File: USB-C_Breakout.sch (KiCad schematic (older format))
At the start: 4 parts

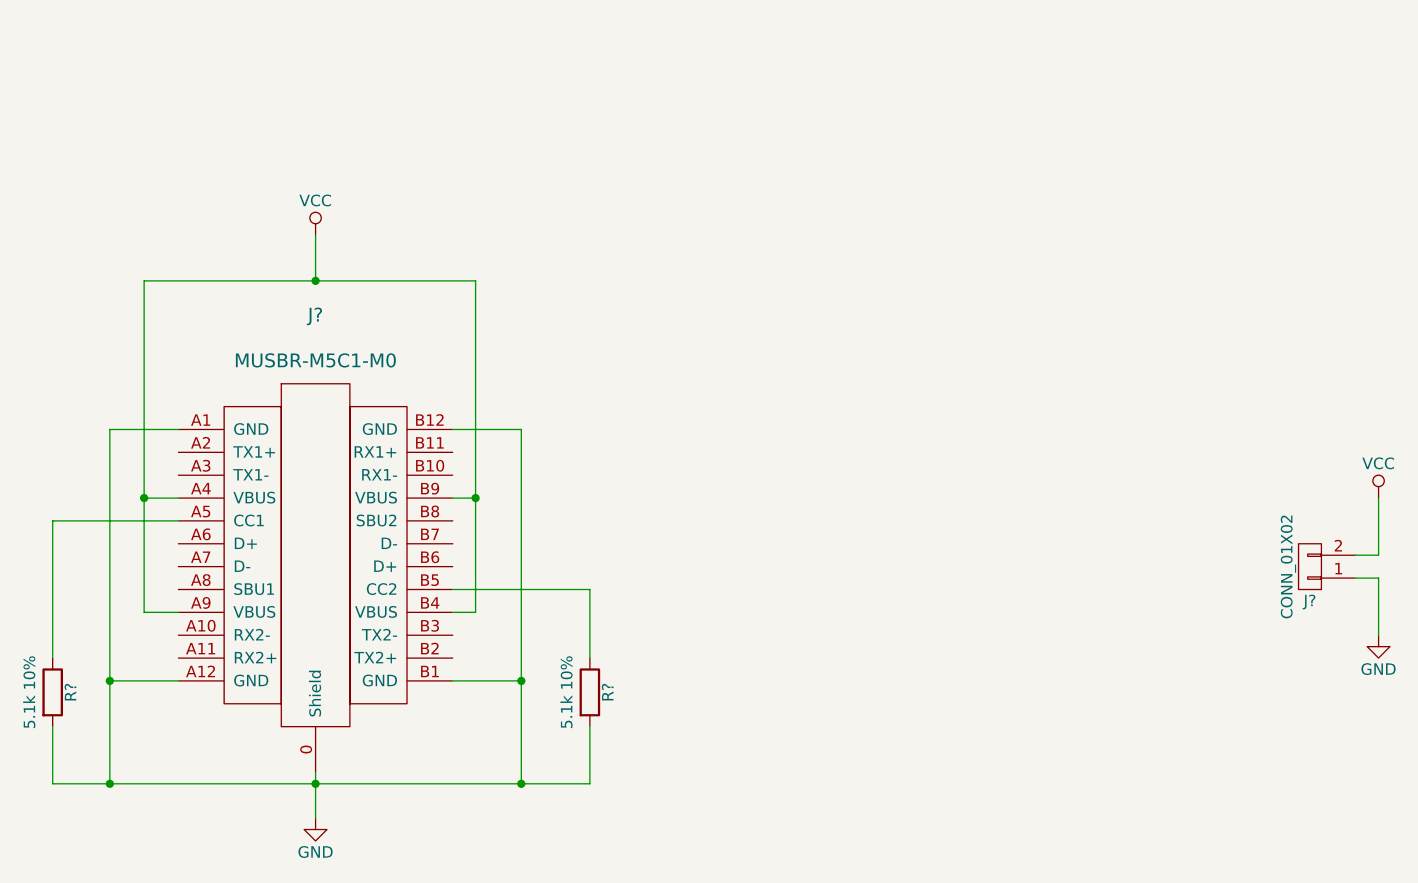
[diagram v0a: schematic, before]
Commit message: Updated Footprints
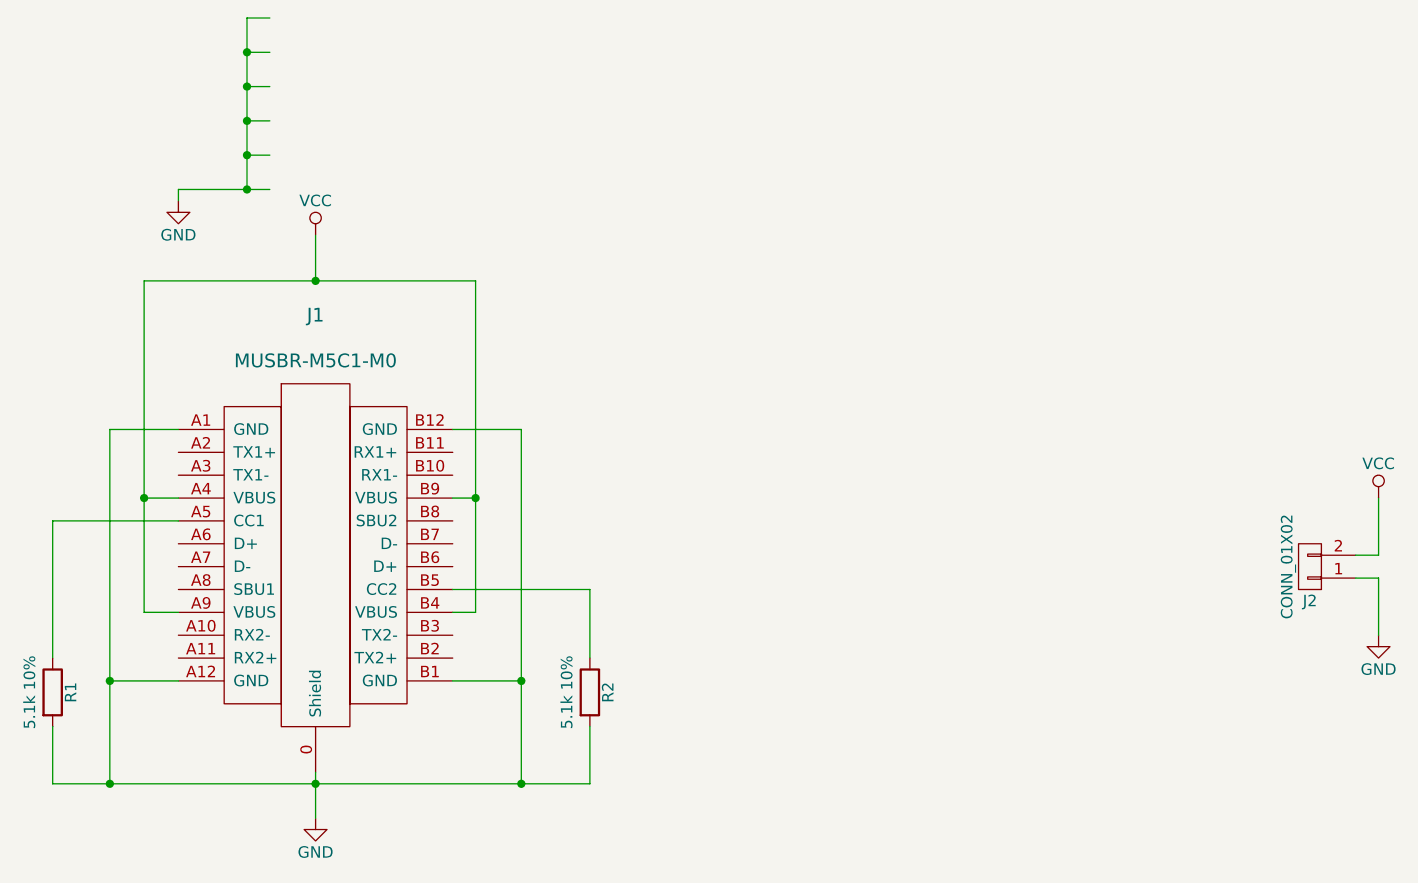
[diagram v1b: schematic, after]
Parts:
- removed R?: 5.1k 10%, symbol R
- added R1: 5.1k 10%, Resistors_SMD:R_0805, symbol R
- J1: renamed from J?; footprint (none) -> MUSBR-M5C1-X0:MUSBR-M5C1-X0
- J2: renamed from J?; footprint (none) -> 640455-2:640455-2
- R2: renamed from R?; footprint (none) -> Resistors_SMD:R_0805
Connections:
- net GND: now also J1.G1 (GND), J1.G2 (GND), J1.G3 (GND), J1.G4 (GND), J1.G5 (GND), J1.G6 (GND), R1.2
- net at J1.A5 (CC1): now also R1.1
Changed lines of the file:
@@
 LIBS:power
 LIBS:device
-LIBS:transistors
-LIBS:conn
-LIBS:linear
-LIBS:regul
 LIBS:74xx
-LIBS:cmos4000
-LIBS:adc-dac
-LIBS:memory
-LIBS:xilinx
-LIBS:microcontrollers
-LIBS:dsp
-LIBS:microchip
-LIBS:analog_switches
-LIBS:motorola
-LIBS:texas
-LIBS:intel
 LIBS:audio
 LIBS:interface
-LIBS:digital-audio
-LIBS:philips
-LIBS:display
-LIBS:cypress
-LIBS:siliconi
-LIBS:opto
-LIBS:atmel
-LIBS:contrib
-LIBS:valves
 LIBS:usb-type-c
+LIBS:USB-C_Breakout-cache
 EELAYER 25 0
 EELAYER END
@@
 $EndDescr
 $Comp
-L USB_TYPE_C J?
+L USB_TYPE_C J1
 U 1 1 5AC3DA60
 P 3550 3350
-F 0 "J?" H 3550 4400 60  0000 C CNN
+F 0 "J1" H 3550 4400 60  0000 C CNN
 F 1 "MUSBR-M5C1-M0" H 3550 4200 60  0000 C CNN
-F 2 "" H 3550 3350 60  0000 C CNN
+F 2 "MUSBR-M5C1-X0:MUSBR-M5C1-X0" H 3550 3350 60  0001 C CNN
 F 3 "" H 3550 3350 60  0000 C CNN
 	1    3550 3350
@@
 $EndComp
 $Comp
-L CONN_01X02 J?
+L CONN_01X02 J2
 U 1 1 5AC3DB4D
 P 7900 3400
-F 0 "J?" H 7900 3550 50  0000 C CNN
+F 0 "J2" H 7900 3550 50  0000 C CNN
 F 1 "CONN_01X02" V 8000 3400 50  0000 C CNN
-F 2 "" H 7900 3400 50  0001 C CNN
+F 2 "640455-2:640455-2" H 7900 3400 50  0001 C CNN
 F 3 "" H 7900 3400 50  0001 C CNN
 	1    7900 3400
@@
 $EndComp
 $Comp
-L R R?
+L R R2
 U 1 1 5AC3DBB4
 P 4750 3950
-F 0 "R?" V 4830 3950 50  0000 C CNN
+F 0 "R2" V 4830 3950 50  0000 C CNN
 F 1 "5.1k 10%" V 4650 3950 50  0000 C CNN
-F 2 "" V 4680 3950 50  0001 C CNN
+F 2 "Resistors_SMD:R_0805" V 4680 3950 50  0001 C CNN
 F 3 "" H 4750 3950 50  0001 C CNN
 	1    4750 3950
@@
 $EndComp
 $Comp
-L VCC #PWR?
+L VCC #PWR2
 U 1 1 5AC3DC66
 P 3550 1950
-F 0 "#PWR?" H 3550 1800 50  0001 C CNN
+F 0 "#PWR2" H 3550 1800 50  0001 C CNN
 F 1 "VCC" H 3550 2100 50  0000 C CNN
 F 2 "" H 3550 1950 50  0001 C CNN
@@
 $EndComp
 $Comp
-L GND #PWR?
+L GND #PWR3
 U 1 1 5AC3DCE0
 P 3550 4500
-F 0 "#PWR?" H 3550 4250 50  0001 C CNN
+F 0 "#PWR3" H 3550 4250 50  0001 C CNN
 F 1 "GND" H 3550 4350 50  0000 C CNN
 F 2 "" H 3550 4500 50  0001 C CNN
@@
 	1    0    0    -1
 $EndComp
-$Comp
-L R R?
-U 1 1 5AC3DFFC
-P 2400 3950
-F 0 "R?" V 2480 3950 50  0000 C CNN
-F 1 "5.1k 10%" V 2300 3950 50  0000 C CNN
-F 2 "" V 2330 3950 50  0001 C CNN
-F 3 "" H 2400 3950 50  0001 C CNN
-	1    2400 3950
-	1    0    0    -1
-$EndComp
 Wire Wire Line
 	3550 4300 3550 4500
@@
 Connection ~ 2650 4350
 $Comp
-L VCC #PWR?
+L VCC #PWR4
 U 1 1 5AC3E2BC
 P 8200 3100
-F 0 "#PWR?" H 8200 2950 50  0001 C CNN
+F 0 "#PWR4" H 8200 2950 50  0001 C CNN
 F 1 "VCC" H 8200 3250 50  0000 C CNN
 F 2 "" H 8200 3100 50  0001 C CNN
@@
 $EndComp
 $Comp
-L GND #PWR?
+L GND #PWR5
 U 1 1 5AC3E2D3
 P 8200 3700
-F 0 "#PWR?" H 8200 3450 50  0001 C CNN
+F 0 "#PWR5" H 8200 3450 50  0001 C CNN
 F 1 "GND" H 8200 3550 50  0000 C CNN
 F 2 "" H 8200 3700 50  0001 C CNN
@@
 Wire Wire Line
 	8200 3450 8200 3700
+$Comp
+L R R1
+U 1 1 5AC3F2EA
+P 2400 3950
+F 0 "R1" V 2480 3950 50  0000 C CNN
+F 1 "5.1k 10%" V 2300 3950 50  0000 C CNN
+F 2 "Resistors_SMD:R_0805" V 2330 3950 50  0001 C CNN
+F 3 "" H 2400 3950 50  0001 C CNN
+	1    2400 3950
+	1    0    0    -1
+$EndComp
+$Comp
+L GND #PWR1
+U 1 1 5AC400B5
+P 2950 1800
+F 0 "#PWR1" H 2950 1550 50  0001 C CNN
+F 1 "GND" H 2950 1650 50  0000 C CNN
+F 2 "" H 2950 1800 50  0001 C CNN
+F 3 "" H 2950 1800 50  0001 C CNN
+	1    2950 1800
+	1    0    0    -1
+$EndComp
+Wire Wire Line
+	3350 1750 2950 1750
+Wire Wire Line
+	2950 1750 2950 1800
+Wire Wire Line
+	3350 1600 3250 1600
+Wire Wire Line
+	3250 1000 3250 1750
+Connection ~ 3250 1750
+Wire Wire Line
+	3350 1450 3250 1450
+Connection ~ 3250 1600
+Wire Wire Line
+	3350 1300 3250 1300
+Connection ~ 3250 1450
+Wire Wire Line
+	3350 1150 3250 1150
+Connection ~ 3250 1300
+Wire Wire Line
+	3350 1000 3250 1000
+Connection ~ 3250 1150
 $EndSCHEMATC

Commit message: Initial Release of Rev A
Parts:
- J2: value CONN_01X02 -> 640455-2
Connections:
- net GND: no longer J1.G1 (GND), J1.G2 (GND), J1.G3 (GND), J1.G4 (GND), J1.G5 (GND), J1.G6 (GND)
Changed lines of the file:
@@
 LIBS:power
 LIBS:device
+LIBS:transistors
+LIBS:conn
+LIBS:linear
+LIBS:regul
 LIBS:74xx
+LIBS:cmos4000
+LIBS:adc-dac
+LIBS:memory
+LIBS:xilinx
+LIBS:microcontrollers
+LIBS:dsp
+LIBS:microchip
+LIBS:analog_switches
+LIBS:motorola
+LIBS:texas
+LIBS:intel
 LIBS:audio
 LIBS:interface
+LIBS:digital-audio
+LIBS:philips
+LIBS:display
+LIBS:cypress
+LIBS:siliconi
+LIBS:opto
+LIBS:atmel
+LIBS:contrib
+LIBS:valves
 LIBS:usb-type-c
 LIBS:USB-C_Breakout-cache
@@
 $EndDescr
 $Comp
+L CONN_01X02 J2
+U 1 1 5AC3DB4D
+P 7900 3400
+F 0 "J2" H 7900 3550 50  0000 C CNN
+F 1 "640455-2" V 8000 3400 50  0000 C CNN
+F 2 "640455-2:640455-2" H 7900 3400 50  0001 C CNN
+F 3 "" H 7900 3400 50  0001 C CNN
+	1    7900 3400
+	-1   0    0    1
+$EndComp
+$Comp
+L R R2
+U 1 1 5AC3DBB4
+P 4750 3950
+F 0 "R2" V 4830 3950 50  0000 C CNN
+F 1 "5.1k 10%" V 4650 3950 50  0000 C CNN
+F 2 "Resistors_SMD:R_0805" V 4680 3950 50  0001 C CNN
+F 3 "" H 4750 3950 50  0001 C CNN
+	1    4750 3950
+	1    0    0    -1
+$EndComp
+$Comp
+L VCC #PWR01
+U 1 1 5AC3DC66
+P 3550 1950
+F 0 "#PWR01" H 3550 1800 50  0001 C CNN
+F 1 "VCC" H 3550 2100 50  0000 C CNN
+F 2 "" H 3550 1950 50  0001 C CNN
+F 3 "" H 3550 1950 50  0001 C CNN
+	1    3550 1950
+	1    0    0    -1
+$EndComp
+$Comp
+L GND #PWR02
+U 1 1 5AC3DCE0
+P 3550 4500
+F 0 "#PWR02" H 3550 4250 50  0001 C CNN
+F 1 "GND" H 3550 4350 50  0000 C CNN
+F 2 "" H 3550 4500 50  0001 C CNN
+F 3 "" H 3550 4500 50  0001 C CNN
+	1    3550 4500
+	1    0    0    -1
+$EndComp
+Wire Wire Line
+	3550 4300 3550 4500
+Wire Wire Line
+	4150 2800 4450 2800
+Wire Wire Line
+	4450 2800 4450 4350
+Wire Wire Line
+	2400 4350 4750 4350
+Connection ~ 3550 4350
+Wire Wire Line
+	2650 2800 2650 4350
+Wire Wire Line
+	2650 2800 2950 2800
+Wire Wire Line
+	4150 3900 4450 3900
+Connection ~ 4450 3900
+Wire Wire Line
+	2950 3900 2650 3900
+Connection ~ 2650 3900
+Wire Wire Line
+	4150 3100 4250 3100
+Wire Wire Line
+	4250 2150 4250 3600
+Wire Wire Line
+	2800 2150 4250 2150
+Wire Wire Line
+	3550 2150 3550 1950
+Wire Wire Line
+	2950 3100 2800 3100
+Wire Wire Line
+	2800 2150 2800 3600
+Connection ~ 3550 2150
+Wire Wire Line
+	4250 3600 4150 3600
+Connection ~ 4250 3100
+Wire Wire Line
+	2800 3600 2950 3600
+Connection ~ 2800 3100
+Wire Wire Line
+	4150 3500 4750 3500
+Wire Wire Line
+	4750 3500 4750 3800
+Wire Wire Line
+	4750 4350 4750 4100
+Connection ~ 4450 4350
+Wire Wire Line
+	2950 3200 2400 3200
+Wire Wire Line
+	2400 3200 2400 3800
+Wire Wire Line
+	2400 4100 2400 4350
+Connection ~ 2650 4350
+$Comp
+L VCC #PWR03
+U 1 1 5AC3E2BC
+P 8200 3100
+F 0 "#PWR03" H 8200 2950 50  0001 C CNN
+F 1 "VCC" H 8200 3250 50  0000 C CNN
+F 2 "" H 8200 3100 50  0001 C CNN
+F 3 "" H 8200 3100 50  0001 C CNN
+	1    8200 3100
+	1    0    0    -1
+$EndComp
+$Comp
+L GND #PWR04
+U 1 1 5AC3E2D3
+P 8200 3700
+F 0 "#PWR04" H 8200 3450 50  0001 C CNN
+F 1 "GND" H 8200 3550 50  0000 C CNN
+F 2 "" H 8200 3700 50  0001 C CNN
+F 3 "" H 8200 3700 50  0001 C CNN
+	1    8200 3700
+	1    0    0    -1
+$EndComp
+Wire Wire Line
+	8100 3350 8200 3350
+Wire Wire Line
+	8200 3350 8200 3100
+Wire Wire Line
+	8100 3450 8200 3450
+Wire Wire Line
+	8200 3450 8200 3700
+$Comp
+L R R1
+U 1 1 5AC3F2EA
+P 2400 3950
+F 0 "R1" V 2480 3950 50  0000 C CNN
+F 1 "5.1k 10%" V 2300 3950 50  0000 C CNN
+F 2 "Resistors_SMD:R_0805" V 2330 3950 50  0001 C CNN
+F 3 "" H 2400 3950 50  0001 C CNN
+	1    2400 3950
+	1    0    0    -1
+$EndComp
+$Comp
 L USB_TYPE_C J1
 U 1 1 5AC3DA60
@@
 $EndComp
 $Comp
-L CONN_01X02 J2
-U 1 1 5AC3DB4D
-P 7900 3400
-F 0 "J2" H 7900 3550 50  0000 C CNN
-F 1 "CONN_01X02" V 8000 3400 50  0000 C CNN
-F 2 "640455-2:640455-2" H 7900 3400 50  0001 C CNN
-F 3 "" H 7900 3400 50  0001 C CNN
-	1    7900 3400
-	-1   0    0    1
-$EndComp
-$Comp
-L R R2
-U 1 1 5AC3DBB4
-P 4750 3950
-F 0 "R2" V 4830 3950 50  0000 C CNN
-F 1 "5.1k 10%" V 4650 3950 50  0000 C CNN
-F 2 "Resistors_SMD:R_0805" V 4680 3950 50  0001 C CNN
-F 3 "" H 4750 3950 50  0001 C CNN
-	1    4750 3950
-	1    0    0    -1
-$EndComp
-$Comp
-L VCC #PWR2
-U 1 1 5AC3DC66
-P 3550 1950
-F 0 "#PWR2" H 3550 1800 50  0001 C CNN
-F 1 "VCC" H 3550 2100 50  0000 C CNN
-F 2 "" H 3550 1950 50  0001 C CNN
-F 3 "" H 3550 1950 50  0001 C CNN
-	1    3550 1950
-	1    0    0    -1
-$EndComp
-$Comp
-L GND #PWR3
-U 1 1 5AC3DCE0
-P 3550 4500
-F 0 "#PWR3" H 3550 4250 50  0001 C CNN
-F 1 "GND" H 3550 4350 50  0000 C CNN
-F 2 "" H 3550 4500 50  0001 C CNN
-F 3 "" H 3550 4500 50  0001 C CNN
-	1    3550 4500
-	1    0    0    -1
-$EndComp
-Wire Wire Line
-	3550 4300 3550 4500
-Wire Wire Line
-	4150 2800 4450 2800
-Wire Wire Line
-	4450 2800 4450 4350
-Wire Wire Line
-	2400 4350 4750 4350
-Connection ~ 3550 4350
-Wire Wire Line
-	2650 2800 2650 4350
-Wire Wire Line
-	2650 2800 2950 2800
-Wire Wire Line
-	4150 3900 4450 3900
-Connection ~ 4450 3900
-Wire Wire Line
-	2950 3900 2650 3900
-Connection ~ 2650 3900
-Wire Wire Line
-	4150 3100 4250 3100
-Wire Wire Line
-	4250 2150 4250 3600
-Wire Wire Line
-	2800 2150 4250 2150
-Wire Wire Line
-	3550 2150 3550 1950
-Wire Wire Line
-	2950 3100 2800 3100
-Wire Wire Line
-	2800 2150 2800 3600
-Connection ~ 3550 2150
-Wire Wire Line
-	4250 3600 4150 3600
-Connection ~ 4250 3100
-Wire Wire Line
-	2800 3600 2950 3600
-Connection ~ 2800 3100
-Wire Wire Line
-	4150 3500 4750 3500
-Wire Wire Line
-	4750 3500 4750 3800
-Wire Wire Line
-	4750 4350 4750 4100
-Connection ~ 4450 4350
-Wire Wire Line
-	2950 3200 2400 3200
-Wire Wire Line
-	2400 3200 2400 3800
-Wire Wire Line
-	2400 4100 2400 4350
-Connection ~ 2650 4350
-$Comp
-L VCC #PWR4
-U 1 1 5AC3E2BC
-P 8200 3100
-F 0 "#PWR4" H 8200 2950 50  0001 C CNN
-F 1 "VCC" H 8200 3250 50  0000 C CNN
-F 2 "" H 8200 3100 50  0001 C CNN
-F 3 "" H 8200 3100 50  0001 C CNN
-	1    8200 3100
-	1    0    0    -1
-$EndComp
-$Comp
-L GND #PWR5
-U 1 1 5AC3E2D3
-P 8200 3700
-F 0 "#PWR5" H 8200 3450 50  0001 C CNN
-F 1 "GND" H 8200 3550 50  0000 C CNN
-F 2 "" H 8200 3700 50  0001 C CNN
-F 3 "" H 8200 3700 50  0001 C CNN
-	1    8200 3700
-	1    0    0    -1
-$EndComp
-Wire Wire Line
-	8100 3350 8200 3350
-Wire Wire Line
-	8200 3350 8200 3100
-Wire Wire Line
-	8100 3450 8200 3450
-Wire Wire Line
-	8200 3450 8200 3700
-$Comp
-L R R1
-U 1 1 5AC3F2EA
-P 2400 3950
-F 0 "R1" V 2480 3950 50  0000 C CNN
-F 1 "5.1k 10%" V 2300 3950 50  0000 C CNN
-F 2 "Resistors_SMD:R_0805" V 2330 3950 50  0001 C CNN
-F 3 "" H 2400 3950 50  0001 C CNN
-	1    2400 3950
-	1    0    0    -1
-$EndComp
-$Comp
-L GND #PWR1
-U 1 1 5AC400B5
-P 2950 1800
-F 0 "#PWR1" H 2950 1550 50  0001 C CNN
-F 1 "GND" H 2950 1650 50  0000 C CNN
-F 2 "" H 2950 1800 50  0001 C CNN
-F 3 "" H 2950 1800 50  0001 C CNN
-	1    2950 1800
-	1    0    0    -1
-$EndComp
-Wire Wire Line
-	3350 1750 2950 1750
-Wire Wire Line
-	2950 1750 2950 1800
-Wire Wire Line
-	3350 1600 3250 1600
-Wire Wire Line
-	3250 1000 3250 1750
-Connection ~ 3250 1750
-Wire Wire Line
-	3350 1450 3250 1450
-Connection ~ 3250 1600
-Wire Wire Line
-	3350 1300 3250 1300
-Connection ~ 3250 1450
-Wire Wire Line
-	3350 1150 3250 1150
-Connection ~ 3250 1300
-Wire Wire Line
-	3350 1000 3250 1000
-Connection ~ 3250 1150
+L PWR_FLAG #FLG?
+U 1 1 5AC519FC
+P 3900 4350
+F 0 "#FLG?" H 3900 4425 50  0001 C CNN
+F 1 "PWR_FLAG" H 3900 4500 50  0000 C CNN
+F 2 "" H 3900 4350 50  0001 C CNN
+F 3 "" H 3900 4350 50  0001 C CNN
+	1    3900 4350
+	1    0    0    -1
+$EndComp
+$Comp
+L PWR_FLAG #FLG?
+U 1 1 5AC51A9E
+P 4250 2150
+F 0 "#FLG?" H 4250 2225 50  0001 C CNN
+F 1 "PWR_FLAG" H 4250 2300 50  0000 C CNN
+F 2 "" H 4250 2150 50  0001 C CNN
+F 3 "" H 4250 2150 50  0001 C CNN
+	1    4250 2150
+	1    0    0    -1
+$EndComp
 $EndSCHEMATC
